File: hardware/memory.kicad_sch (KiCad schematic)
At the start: 15 parts, among them U10 IS42S16320D-6BLI, U4 GateMate-CCGM1A1

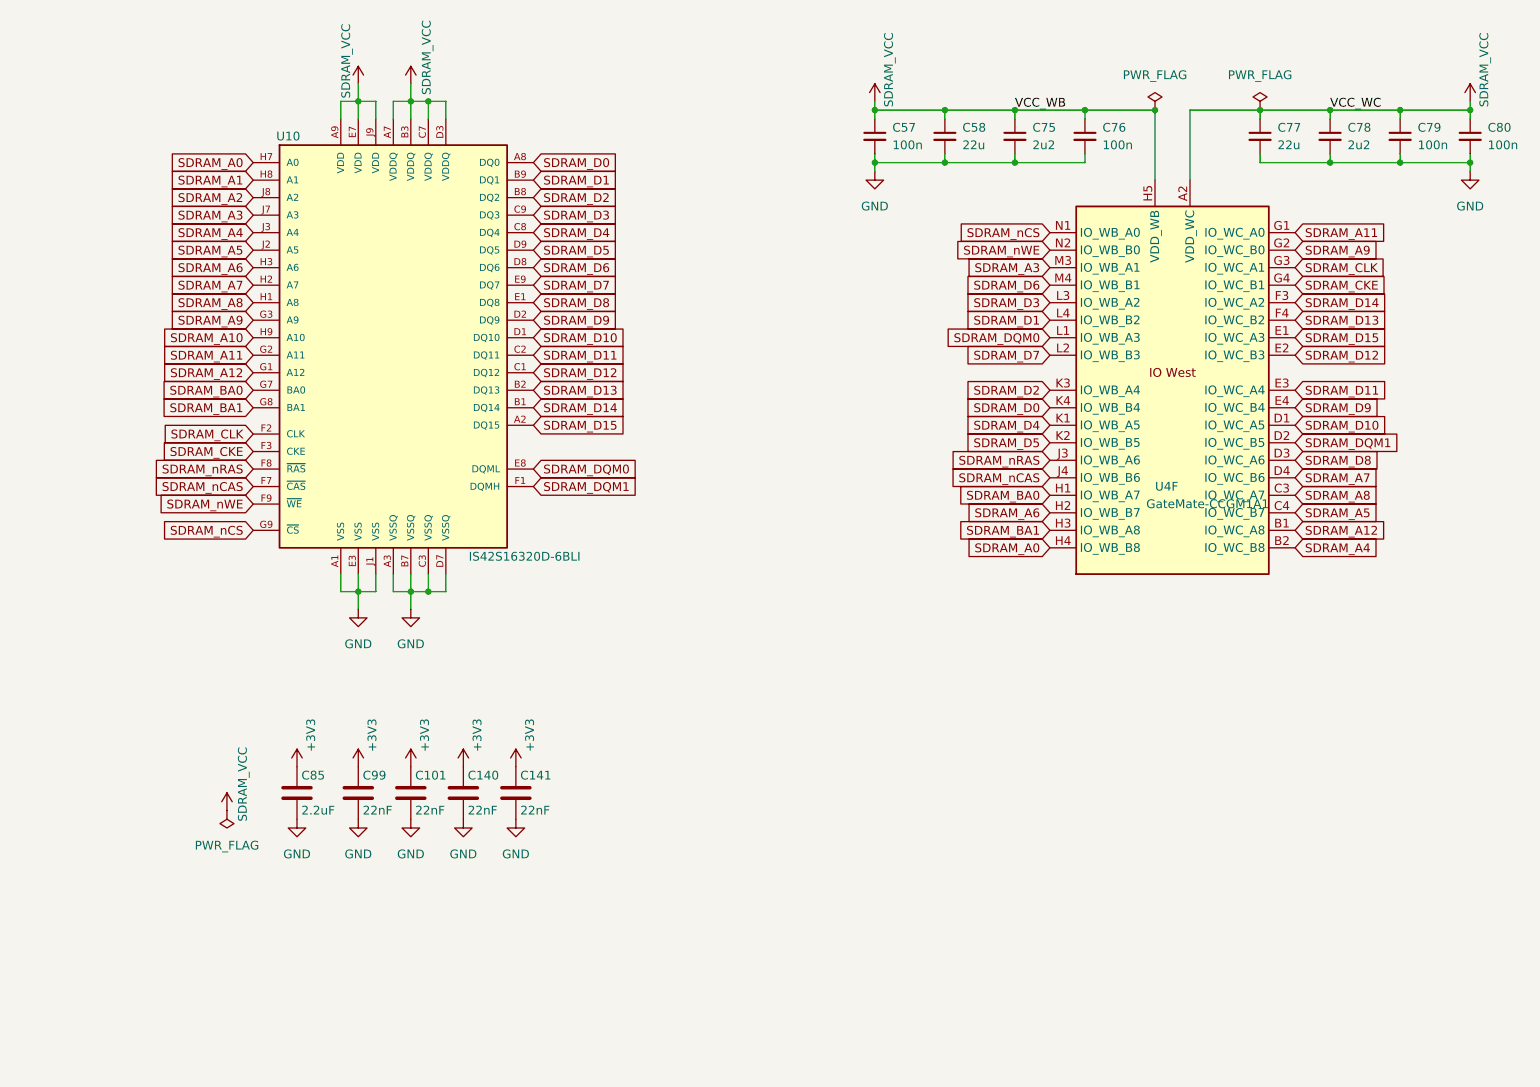
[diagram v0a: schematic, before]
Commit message: ram: rename to memory, switch to hyperram
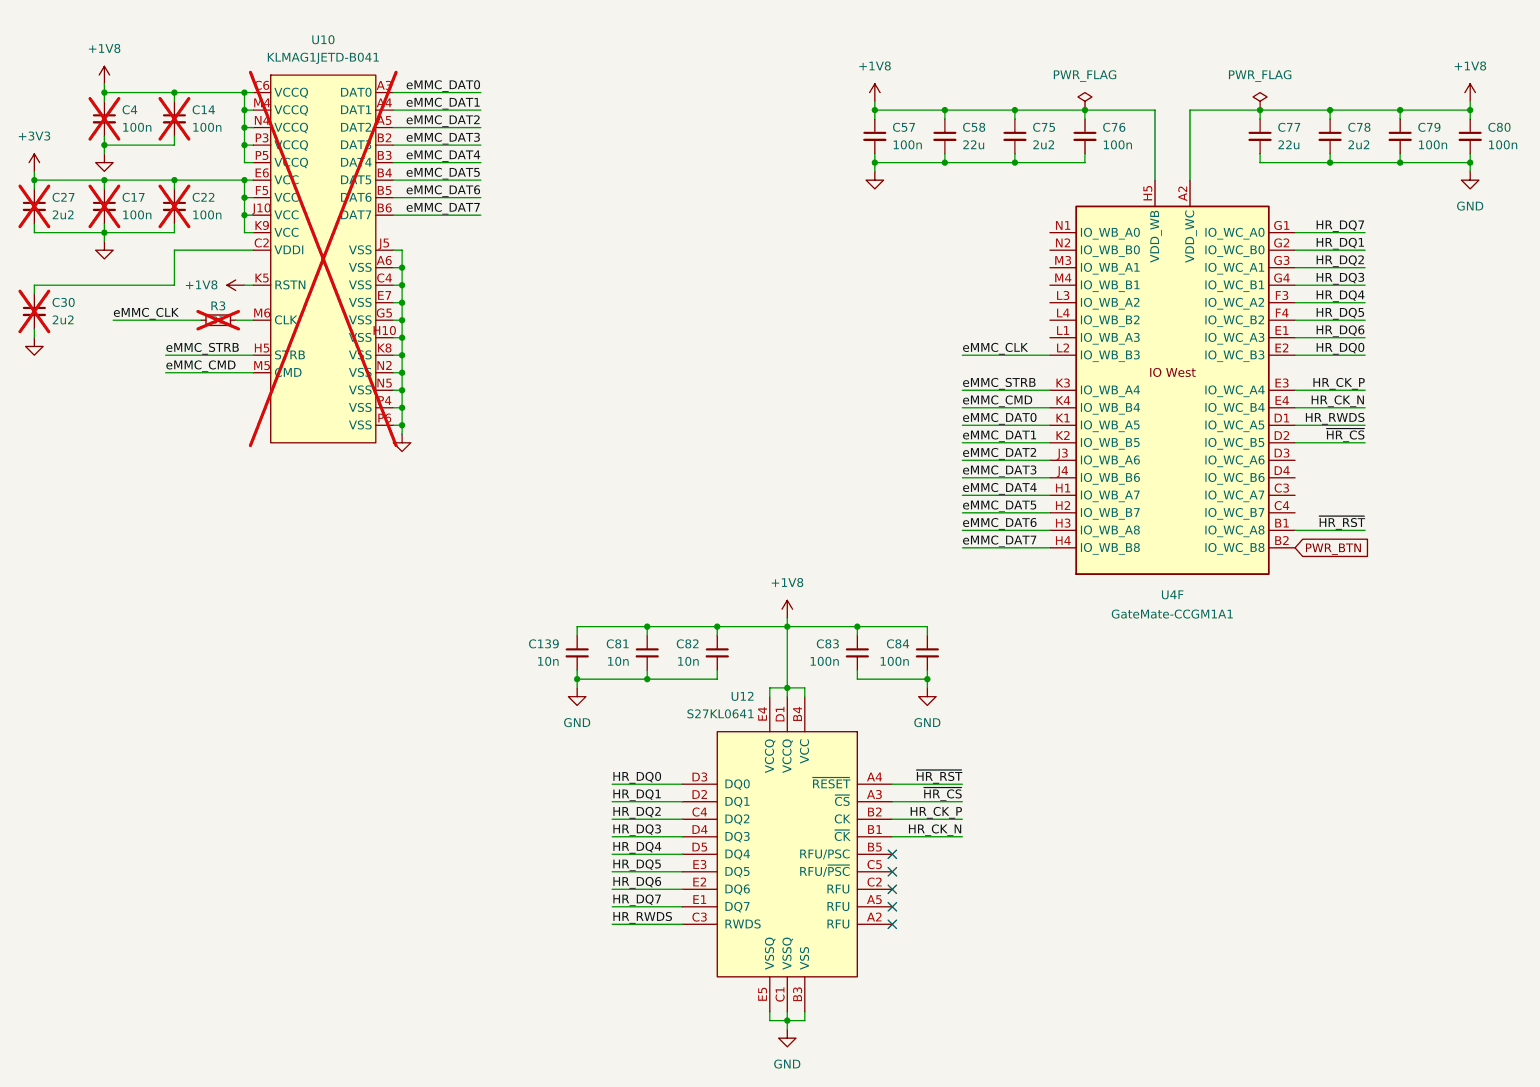
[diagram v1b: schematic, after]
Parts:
- removed C101, C140, C141, C99: 22nF, Capacitor_SMD:C_0402_1005Metric, symbol Device:C
- removed C85: 2.2uF, Capacitor_SMD:C_0402_1005Metric, symbol Device:C
- removed U10: IS42S16320D-6BLI, IS42S16320D:IS42S16320D-6BLI, symbol mt48lc16m16a2tg:IS42S16320D-6BLI
- added C139, C81, C82: 10n, Capacitor_SMD:C_0402_1005Metric, symbol Device:C_Small
- added C14, C17, C22, C4, C83, C84: 100n, Capacitor_SMD:C_0402_1005Metric, symbol Device:C_Small
- added C27, C30: 2u2, Capacitor_SMD:C_0402_1005Metric, symbol Device:C_Small
- added R3: 33, Resistor_SMD:R_0402_1005Metric, symbol Device:R_Small
- added U10: KLMAG1JETD-B041, Package_BGA:LFBGA-153_11.5x13mm_Layout14x14_P0.5mm, symbol CM5:KLMAG1JETD-B041
- added U12: S27KL0641, Package_BGA:BGA-24_6x8mm_Layout5x5_P1.0mm, symbol HyperRAM:S27KL0641
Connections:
- net +3V3: now also C17.1, C22.1, C27.1, U10.E6 (VCC), U10.F5 (VCC), U10.J10 (VCC), U10.K9 (VCC)
- net GND: now also C139.2, C14.2, C17.2, C22.2, C27.2, C30.2, C4.2, C81.2, C82.2, C83.2, C84.2, U10.A6 (VSS), U10.C4 (VSS), U10.E7 (VSS), U10.G5 (VSS), U10.H10 (VSS), U10.J5 (VSS), U10.K8 (VSS), U10.N2 (VSS), U10.N5 (VSS), U10.P4 (VSS), U10.P6 (VSS), U12.B3 (VSS), U12.C1 (VSSQ), U12.E5 (VSSQ)
- net SDRAM_A0 renamed eMMC_DAT7
- net eMMC_DAT7: now also U10.B6 (DAT7)
- net SDRAM_A11 renamed HR_DQ7
- net HR_DQ7: now also U12.E1 (DQ7)
- net SDRAM_A12 renamed ~{HR_RST}
- net ~{HR_RST}: now also U12.A4 (~{RESET})
- net SDRAM_A3: no longer names the net of U4.M3 (IO_WB_A1)
- net SDRAM_A4 renamed PWR_BTN
- net SDRAM_A5: no longer names the net of U4.C4 (IO_WC_B7)
- net SDRAM_A6 renamed eMMC_DAT5
- net eMMC_DAT5: now also U10.B4 (DAT5)
- net SDRAM_A7: no longer names the net of U4.D4 (IO_WC_B6)
- net SDRAM_A8: no longer names the net of U4.C3 (IO_WC_A7)
- net SDRAM_A9 renamed HR_DQ1
- net HR_DQ1: now also U12.D2 (DQ1)
- net SDRAM_BA0 renamed eMMC_DAT4
- net eMMC_DAT4: now also U10.B3 (DAT4)
- net SDRAM_BA1 renamed eMMC_DAT6
- net eMMC_DAT6: now also U10.B5 (DAT6)
- net SDRAM_CKE renamed HR_DQ3
- net HR_DQ3: now also U12.D4 (DQ3)
- net SDRAM_CLK renamed HR_DQ2
- net HR_DQ2: now also U12.C4 (DQ2)
- net SDRAM_D0 renamed eMMC_CMD
- net eMMC_CMD: now also U10.M5 (CMD)
- net SDRAM_D1: no longer names the net of U4.L4 (IO_WB_B2)
- net SDRAM_D10 renamed HR_RWDS
- net HR_RWDS: now also U12.C3 (RWDS)
- net SDRAM_D11 renamed HR_CK_P
- net HR_CK_P: now also U12.B2 (CK)
- net SDRAM_D12 renamed HR_DQ0
- net HR_DQ0: now also U12.D3 (DQ0)
- net SDRAM_D13 renamed HR_DQ5
- net HR_DQ5: now also U12.E3 (DQ5)
- net SDRAM_D14 renamed HR_DQ4
- net HR_DQ4: now also U12.D5 (DQ4)
- net SDRAM_D15 renamed HR_DQ6
- net HR_DQ6: now also U12.E2 (DQ6)
- net SDRAM_D2 renamed eMMC_STRB
- net eMMC_STRB: now also U10.H5 (STRB)
- net SDRAM_D3: no longer names the net of U4.L3 (IO_WB_A2)
- net SDRAM_D4 renamed eMMC_DAT0
- net eMMC_DAT0: now also U10.A3 (DAT0)
- net SDRAM_D5 renamed eMMC_DAT1
- net eMMC_DAT1: now also U10.A4 (DAT1)
- net SDRAM_D6: no longer names the net of U4.M4 (IO_WB_B1)
- net SDRAM_D7 renamed eMMC_CLK
- net eMMC_CLK: now also R3.2
- net SDRAM_D8: no longer names the net of U4.D3 (IO_WC_A6)
- net SDRAM_D9 renamed HR_CK_N
- net HR_CK_N: now also U12.B1 (~{CK})
- net SDRAM_DQM0: no longer names the net of U4.L1 (IO_WB_A3)
- net SDRAM_DQM1 renamed ~{HR_CS}
- net ~{HR_CS}: now also U12.A3 (~{CS})
- net SDRAM_VCC renamed +1V8
- net +1V8: now also C139.1, C14.1, C4.1, C81.1, C82.1, C83.1, C84.1, U10.C6 (VCCQ), U10.K5 (RSTN), U10.M4 (VCCQ), U10.N4 (VCCQ), U10.P3 (VCCQ), U10.P5 (VCCQ), U12.B4 (VCC), U12.D1 (VCCQ), U12.E4 (VCCQ)
- net SDRAM_nCAS renamed eMMC_DAT3
- net eMMC_DAT3: now also U10.B2 (DAT3)
- net SDRAM_nCS: no longer names the net of U4.N1 (IO_WB_A0)
- net SDRAM_nRAS renamed eMMC_DAT2
- net eMMC_DAT2: now also U10.A5 (DAT2)
- net SDRAM_nWE: no longer names the net of U4.N2 (IO_WB_B0)
- new net: R3.1, U10.M6 (CLK)
- new net: C30.1, U10.C2 (VDDI)
- no-connect marks 0 -> 5
